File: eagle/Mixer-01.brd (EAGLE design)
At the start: 95 x 72 mm, 58 parts, among them IC1 TL072P, IC2 TL072P, IC3 LM4558N

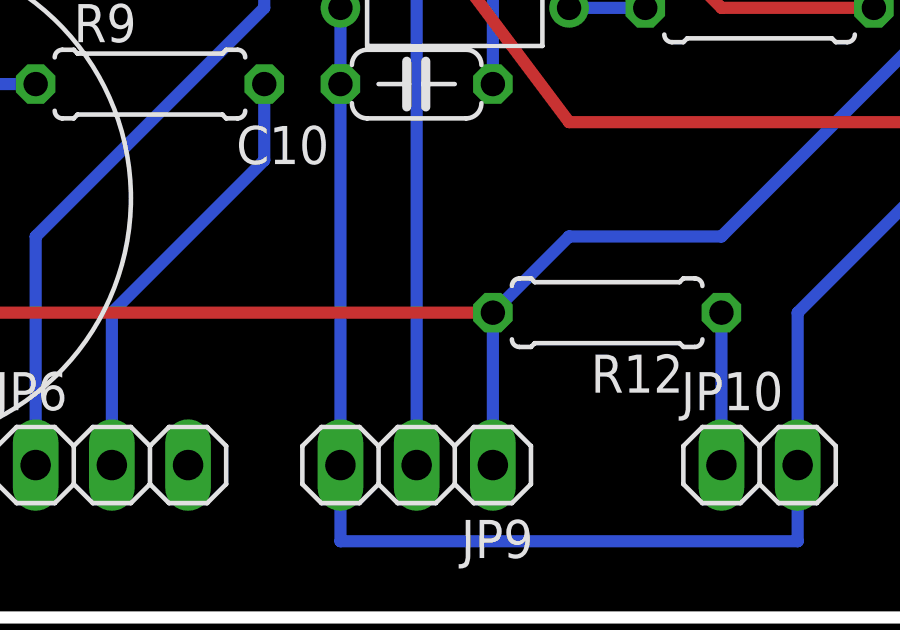
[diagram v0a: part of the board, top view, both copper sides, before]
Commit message: 電池ボックスのGNDの配線を変更
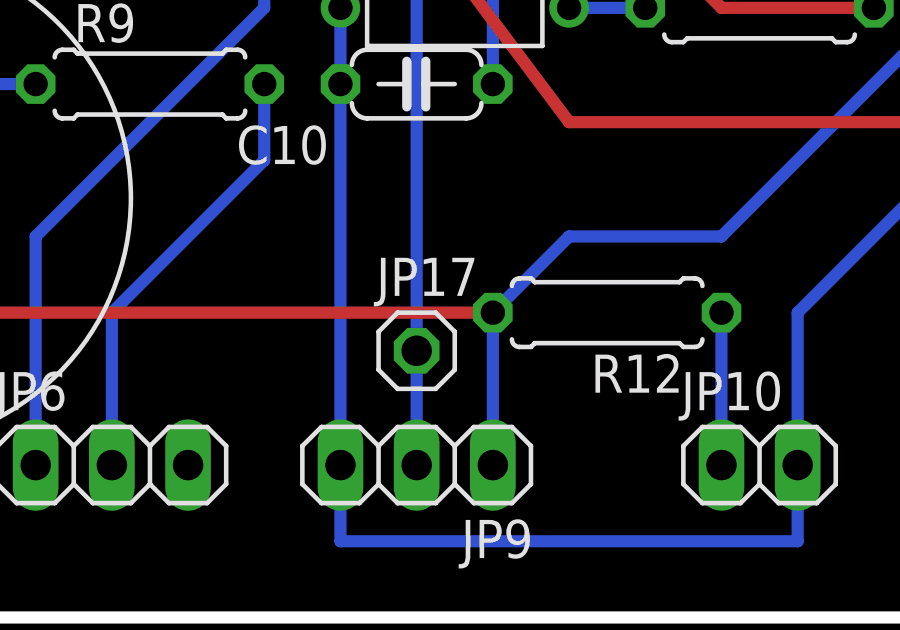
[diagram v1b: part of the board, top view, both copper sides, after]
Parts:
- added JP17: PWR-GND, pinhead:1X01
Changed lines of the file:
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@@
 <element name="R23" library="resistor" package="0207/7" value="47" x="80.01" y="33.02"/>
 <element name="JP16" library="pinhead" package="1X03" value="VOL-R" x="66.04" y="5.08"/>
+<element name="JP17" library="pinhead" package="1X01" value="PWR-GND" x="45.72" y="8.89"/>
 </elements>
 <signals>

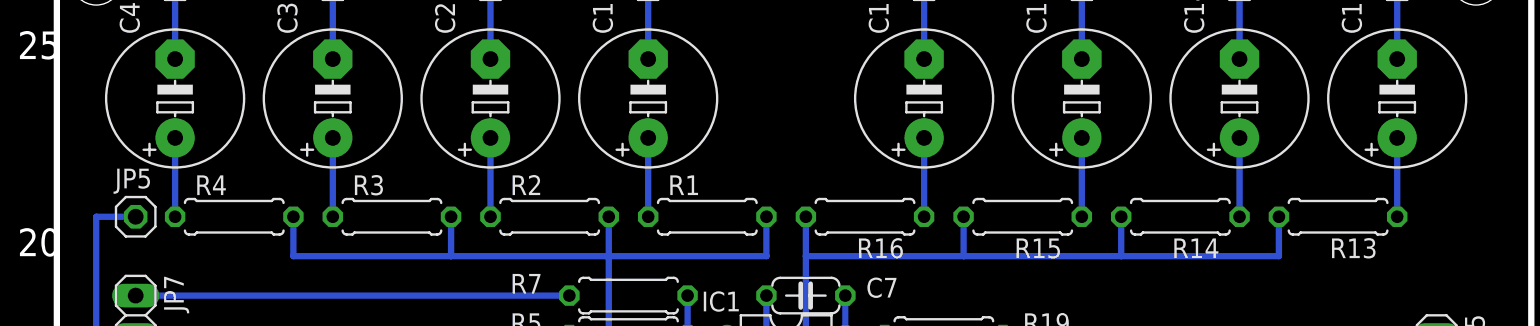
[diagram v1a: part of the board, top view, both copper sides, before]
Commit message: OPAMPの入力を接地
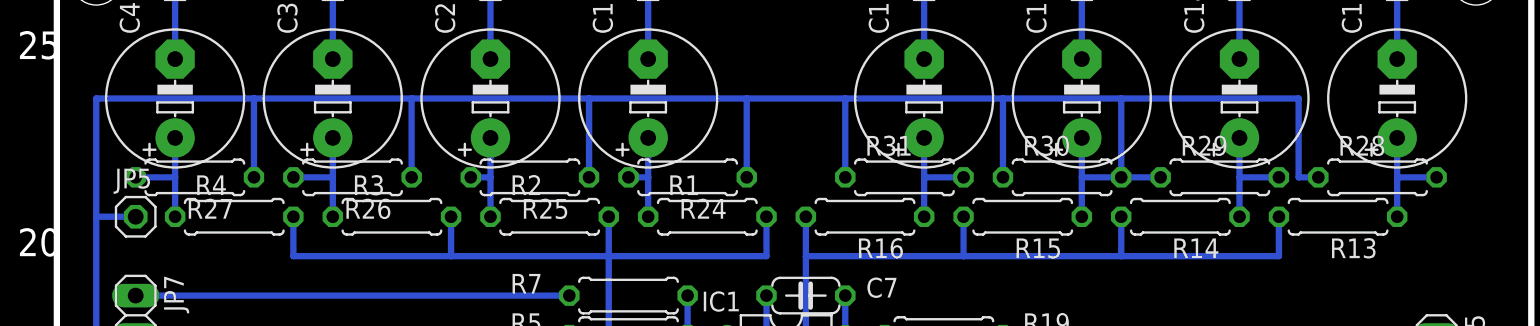
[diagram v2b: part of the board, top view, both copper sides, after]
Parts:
- added R24, R25, R26, R27, R28, R29, R30, R31: 100k, rcl:0207/7
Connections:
- net GND: now also R24.1, R25.1, R26.1, R27.1, R28.1, R29.1, R30.1, R31.1
- net N$10: now also R25.2
- net N$11: now also R26.2
- net N$12: now also R27.2
- net N$18: now also R30.2
- net N$23: now also R31.2
- net N$7: now also R28.2
- net N$8: now also R29.2
- net N$9: now also R24.2
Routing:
- net GND: track 263.0 -> 392.6 mm
- net N$7: track 5.08 -> 7.62 mm
- net N$11: track 5.08 -> 7.62 mm
- net N$12: track 5.08 -> 7.62 mm
- net N$23: track 5.08 -> 7.62 mm
- net N$8: track 5.08 -> 7.62 mm
- net N$18: track 5.08 -> 7.62 mm
- net N$9: track 5.08 -> 6.35 mm
- net N$10: track 5.08 -> 6.35 mm
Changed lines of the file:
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@@
 <layer number="97" name="Info" color="7" fill="1" visible="no" active="no"/>
 <layer number="98" name="Guide" color="6" fill="1" visible="no" active="no"/>
-<layer number="100" name="Grid" color="7" fill="1" visible="yes" active="yes"/>
+<layer number="100" name="Grid" color="7" fill="1" visible="no" active="yes"/>
 <layer number="101" name="Jumper" color="14" fill="1" visible="yes" active="yes"/>
 <layer number="102" name="outline" color="15" fill="1" visible="yes" active="yes"/>
@@
 <element name="JP16" library="pinhead" package="1X03" value="VOL-R" x="66.04" y="5.08"/>
 <element name="JP17" library="pinhead" package="1X01" value="PWR-GND" x="45.72" y="8.89"/>
+<element name="R24" library="rcl" package="0207/7" value="100k" x="40.64" y="55.88" rot="R180"/>
+<element name="R25" library="rcl" package="0207/7" value="100k" x="30.48" y="55.88" rot="R180"/>
+<element name="R26" library="rcl" package="0207/7" value="100k" x="19.05" y="55.88" rot="R180"/>
+<element name="R27" library="rcl" package="0207/7" value="100k" x="8.89" y="55.88" rot="R180"/>
+<element name="R28" library="rcl" package="0207/7" value="100k" x="85.09" y="55.88"/>
+<element name="R29" library="rcl" package="0207/7" value="100k" x="74.93" y="55.88"/>
+<element name="R30" library="rcl" package="0207/7" value="100k" x="64.77" y="55.88"/>
+<element name="R31" library="rcl" package="0207/7" value="100k" x="54.61" y="55.88"/>
 </elements>
 <signals>
@@
 <wire x1="91.44" y1="43.18" x2="88.9" y2="43.18" width="0.4064" layer="16"/>
 <wire x1="48.26" y1="35.56" x2="45.72" y2="35.56" width="0.4064" layer="16"/>
-<wire x1="5.08" y1="53.34" x2="2.54" y2="53.34" width="0.4064" layer="16"/>
 <wire x1="2.54" y1="53.34" x2="2.54" y2="45.72" width="0.4064" layer="16"/>
 <wire x1="2.54" y1="45.72" x2="5.08" y2="45.72" width="0.4064" layer="16"/>
@@
 <wire x1="27.94" y1="27.94" x2="22.86" y2="27.94" width="0.4064" layer="16"/>
 <wire x1="22.86" y1="27.94" x2="5.08" y2="45.72" width="0.4064" layer="16"/>
+<contactref element="R24" pad="1"/>
+<contactref element="R25" pad="1"/>
+<contactref element="R26" pad="1"/>
+<contactref element="R27" pad="1"/>
+<contactref element="R28" pad="1"/>
+<contactref element="R29" pad="1"/>
+<contactref element="R30" pad="1"/>
+<contactref element="R31" pad="1"/>
+<wire x1="5.08" y1="53.34" x2="2.54" y2="53.34" width="0.4064" layer="16"/>
+<wire x1="2.54" y1="53.34" x2="2.54" y2="60.96" width="0.4064" layer="16"/>
+<wire x1="2.54" y1="60.96" x2="12.7" y2="60.96" width="0.4064" layer="16"/>
+<wire x1="12.7" y1="60.96" x2="12.7" y2="55.88" width="0.4064" layer="16"/>
+<wire x1="22.86" y1="55.88" x2="22.86" y2="60.96" width="0.4064" layer="16"/>
+<wire x1="22.86" y1="60.96" x2="12.7" y2="60.96" width="0.4064" layer="16"/>
+<wire x1="34.29" y1="55.88" x2="34.29" y2="60.96" width="0.4064" layer="16"/>
+<wire x1="34.29" y1="60.96" x2="22.86" y2="60.96" width="0.4064" layer="16"/>
+<wire x1="44.45" y1="55.88" x2="44.45" y2="60.96" width="0.4064" layer="16"/>
+<wire x1="44.45" y1="60.96" x2="34.29" y2="60.96" width="0.4064" layer="16"/>
+<wire x1="50.8" y1="55.88" x2="50.8" y2="60.96" width="0.4064" layer="16"/>
+<wire x1="50.8" y1="60.96" x2="44.45" y2="60.96" width="0.4064" layer="16"/>
+<wire x1="60.96" y1="55.88" x2="60.96" y2="60.96" width="0.4064" layer="16"/>
+<wire x1="60.96" y1="60.96" x2="50.8" y2="60.96" width="0.4064" layer="16"/>
+<wire x1="71.12" y1="55.88" x2="68.58" y2="55.88" width="0.4064" layer="16"/>
+<wire x1="68.58" y1="55.88" x2="68.58" y2="60.96" width="0.4064" layer="16"/>
+<wire x1="68.58" y1="60.96" x2="60.96" y2="60.96" width="0.4064" layer="16"/>
+<wire x1="81.28" y1="55.88" x2="80.01" y2="55.88" width="0.4064" layer="16"/>
+<wire x1="80.01" y1="55.88" x2="80.01" y2="60.96" width="0.4064" layer="16"/>
+<wire x1="80.01" y1="60.96" x2="68.58" y2="60.96" width="0.4064" layer="16"/>
 </signal>
 <signal name="N$9">
 <contactref element="C1" pad="+"/>
 <contactref element="R1" pad="1"/>
-<wire x1="38.1" y1="58.42" x2="38.1" y2="53.34" width="0.4064" layer="16"/>
+<wire x1="38.1" y1="58.42" x2="38.1" y2="55.88" width="0.4064" layer="16"/>
+<contactref element="R24" pad="2"/>
+<wire x1="38.1" y1="55.88" x2="38.1" y2="53.34" width="0.4064" layer="16"/>
+<wire x1="36.83" y1="55.88" x2="38.1" y2="55.88" width="0.4064" layer="16"/>
 </signal>
 <signal name="N$10">
 <contactref element="C2" pad="+"/>
 <contactref element="R2" pad="1"/>
-<wire x1="27.94" y1="58.42" x2="27.94" y2="53.34" width="0.4064" layer="16"/>
+<wire x1="27.94" y1="58.42" x2="27.94" y2="55.88" width="0.4064" layer="16"/>
+<contactref element="R25" pad="2"/>
+<wire x1="27.94" y1="55.88" x2="27.94" y2="53.34" width="0.4064" layer="16"/>
+<wire x1="26.67" y1="55.88" x2="27.94" y2="55.88" width="0.4064" layer="16"/>
 </signal>
 <signal name="N$11">
 <contactref element="C3" pad="+"/>
 <contactref element="R3" pad="1"/>
-<wire x1="17.78" y1="58.42" x2="17.78" y2="53.34" width="0.4064" layer="16"/>
+<wire x1="17.78" y1="58.42" x2="17.78" y2="55.88" width="0.4064" layer="16"/>
+<contactref element="R26" pad="2"/>
+<wire x1="17.78" y1="55.88" x2="17.78" y2="53.34" width="0.4064" layer="16"/>
+<wire x1="15.24" y1="55.88" x2="17.78" y2="55.88" width="0.4064" layer="16"/>
 </signal>
 <signal name="N$12">
 <contactref element="C4" pad="+"/>
 <contactref element="R4" pad="1"/>
-<wire x1="7.62" y1="58.42" x2="7.62" y2="53.34" width="0.4064" layer="16"/>
+<wire x1="7.62" y1="58.42" x2="7.62" y2="55.88" width="0.4064" layer="16"/>
+<contactref element="R27" pad="2"/>
+<wire x1="7.62" y1="55.88" x2="7.62" y2="53.34" width="0.4064" layer="16"/>
+<wire x1="5.08" y1="55.88" x2="7.62" y2="55.88" width="0.4064" layer="16"/>
 </signal>
 <signal name="N$13">
@@
 <contactref element="C13" pad="+"/>
 <contactref element="R13" pad="1"/>
-<wire x1="86.36" y1="58.42" x2="86.36" y2="53.34" width="0.4064" layer="16"/>
+<wire x1="86.36" y1="58.42" x2="86.36" y2="55.88" width="0.4064" layer="16"/>
+<contactref element="R28" pad="2"/>
+<wire x1="86.36" y1="55.88" x2="86.36" y2="53.34" width="0.4064" layer="16"/>
+<wire x1="88.9" y1="55.88" x2="86.36" y2="55.88" width="0.4064" layer="16"/>
 </signal>
 <signal name="N$8">
 <contactref element="C14" pad="+"/>
 <contactref element="R14" pad="1"/>
-<wire x1="76.2" y1="58.42" x2="76.2" y2="53.34" width="0.4064" layer="16"/>
+<wire x1="76.2" y1="58.42" x2="76.2" y2="55.88" width="0.4064" layer="16"/>
+<contactref element="R29" pad="2"/>
+<wire x1="76.2" y1="55.88" x2="76.2" y2="53.34" width="0.4064" layer="16"/>
+<wire x1="78.74" y1="55.88" x2="76.2" y2="55.88" width="0.4064" layer="16"/>
 </signal>
 <signal name="N$18">
 <contactref element="C15" pad="+"/>
 <contactref element="R15" pad="1"/>
-<wire x1="66.04" y1="58.42" x2="66.04" y2="53.34" width="0.4064" layer="16"/>
+<wire x1="66.04" y1="58.42" x2="66.04" y2="55.88" width="0.4064" layer="16"/>
+<contactref element="R30" pad="2"/>
+<wire x1="66.04" y1="55.88" x2="66.04" y2="53.34" width="0.4064" layer="16"/>
+<wire x1="68.58" y1="55.88" x2="66.04" y2="55.88" width="0.4064" layer="16"/>
 </signal>
 <signal name="N$23">
 <contactref element="C16" pad="+"/>
 <contactref element="R16" pad="1"/>
-<wire x1="55.88" y1="58.42" x2="55.88" y2="53.34" width="0.4064" layer="16"/>
+<wire x1="55.88" y1="58.42" x2="55.88" y2="55.88" width="0.4064" layer="16"/>
+<contactref element="R31" pad="2"/>
+<wire x1="55.88" y1="55.88" x2="55.88" y2="53.34" width="0.4064" layer="16"/>
+<wire x1="58.42" y1="55.88" x2="55.88" y2="55.88" width="0.4064" layer="16"/>
 </signal>
 <signal name="N$24">

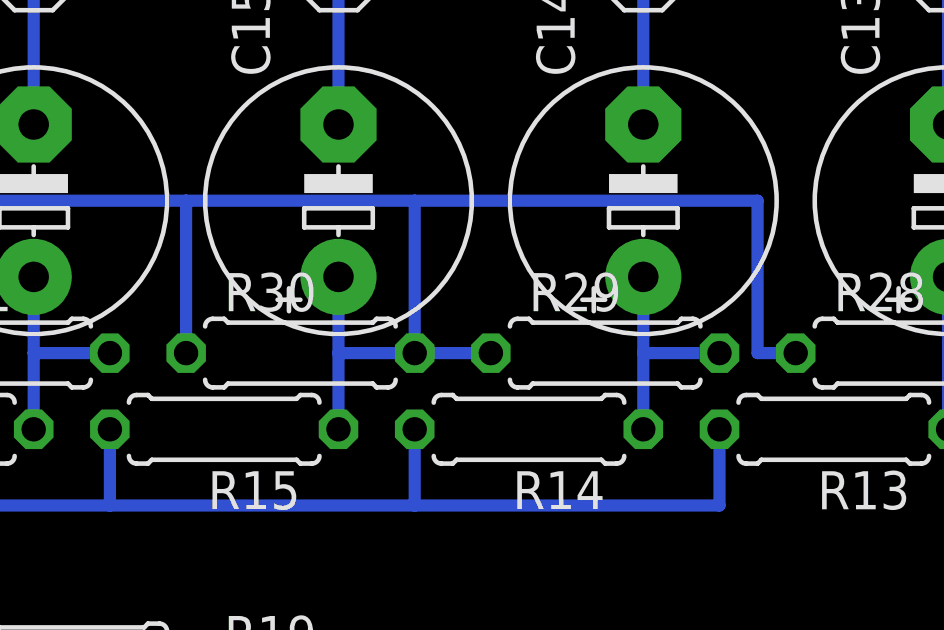
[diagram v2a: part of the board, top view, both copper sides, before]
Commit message: Mixer-01.brd: 配線を修正
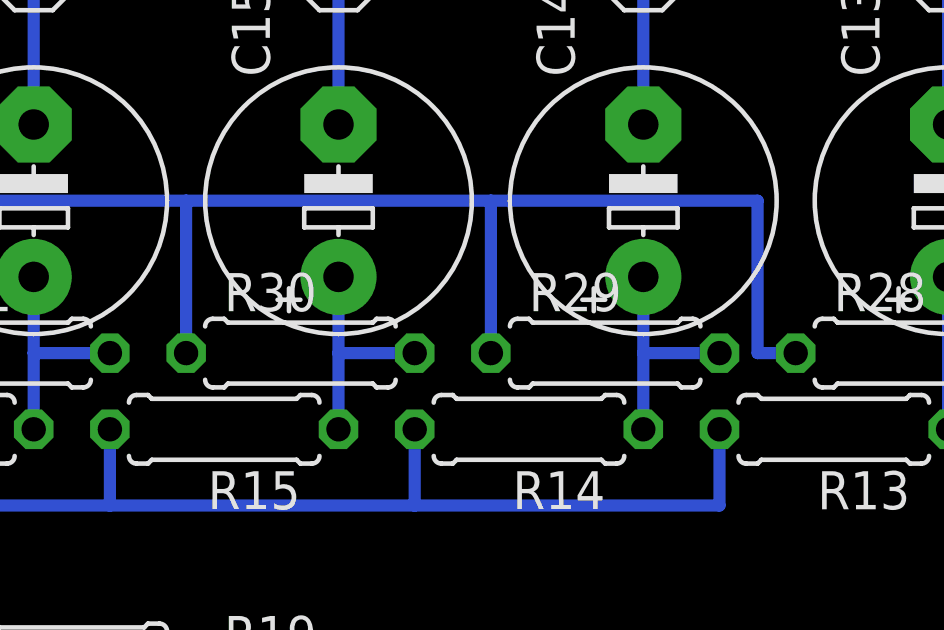
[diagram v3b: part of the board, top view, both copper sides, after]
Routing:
- net GND: track 392.6 -> 390.0 mm
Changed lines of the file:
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@@
 <wire x1="60.96" y1="55.88" x2="60.96" y2="60.96" width="0.4064" layer="16"/>
 <wire x1="60.96" y1="60.96" x2="50.8" y2="60.96" width="0.4064" layer="16"/>
-<wire x1="71.12" y1="55.88" x2="68.58" y2="55.88" width="0.4064" layer="16"/>
-<wire x1="68.58" y1="55.88" x2="68.58" y2="60.96" width="0.4064" layer="16"/>
-<wire x1="68.58" y1="60.96" x2="60.96" y2="60.96" width="0.4064" layer="16"/>
 <wire x1="81.28" y1="55.88" x2="80.01" y2="55.88" width="0.4064" layer="16"/>
 <wire x1="80.01" y1="55.88" x2="80.01" y2="60.96" width="0.4064" layer="16"/>
-<wire x1="80.01" y1="60.96" x2="68.58" y2="60.96" width="0.4064" layer="16"/>
+<wire x1="80.01" y1="60.96" x2="71.12" y2="60.96" width="0.4064" layer="16"/>
+<wire x1="71.12" y1="60.96" x2="60.96" y2="60.96" width="0.4064" layer="16"/>
+<wire x1="71.12" y1="55.88" x2="71.12" y2="60.96" width="0.4064" layer="16"/>
 </signal>
 <signal name="N$9">
@@
 <contactref element="C14" pad="+"/>
 <contactref element="R14" pad="1"/>
-<wire x1="76.2" y1="58.42" x2="76.2" y2="55.88" width="0.4064" layer="16"/>
 <contactref element="R29" pad="2"/>
-<wire x1="76.2" y1="55.88" x2="76.2" y2="53.34" width="0.4064" layer="16"/>
+<wire x1="76.2" y1="53.34" x2="76.2" y2="55.88" width="0.4064" layer="16"/>
+<wire x1="76.2" y1="55.88" x2="76.2" y2="58.42" width="0.4064" layer="16"/>
 <wire x1="78.74" y1="55.88" x2="76.2" y2="55.88" width="0.4064" layer="16"/>
 </signal>
@@
 <contactref element="C15" pad="+"/>
 <contactref element="R15" pad="1"/>
+<contactref element="R30" pad="2"/>
 <wire x1="66.04" y1="58.42" x2="66.04" y2="55.88" width="0.4064" layer="16"/>
-<contactref element="R30" pad="2"/>
 <wire x1="66.04" y1="55.88" x2="66.04" y2="53.34" width="0.4064" layer="16"/>
 <wire x1="68.58" y1="55.88" x2="66.04" y2="55.88" width="0.4064" layer="16"/>

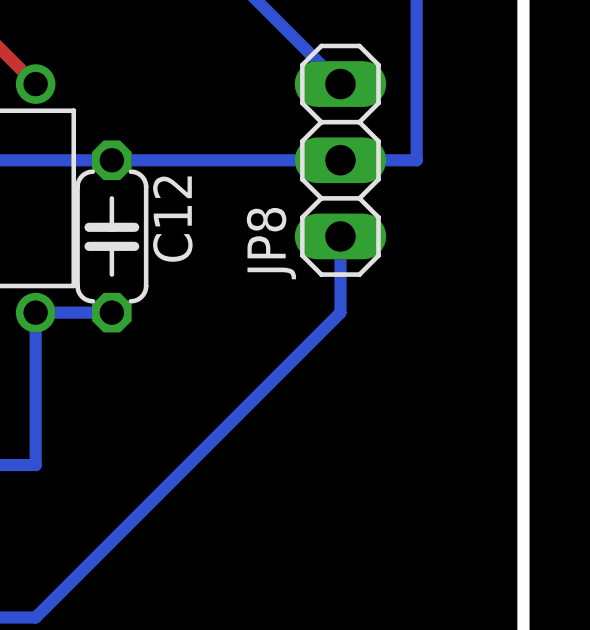
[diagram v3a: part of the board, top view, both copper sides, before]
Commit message: Mixer基板設計図にV-GND用ピンを追加
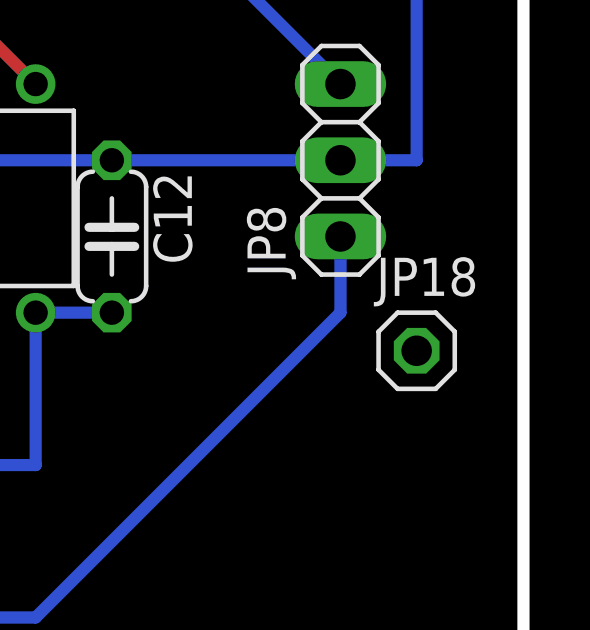
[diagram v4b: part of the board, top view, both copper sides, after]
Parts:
- added JP18: V-GND, pinhead:1X01
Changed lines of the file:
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@@
 <element name="R30" library="rcl" package="0207/7" value="100k" x="64.77" y="55.88"/>
 <element name="R31" library="rcl" package="0207/7" value="100k" x="54.61" y="55.88"/>
+<element name="JP18" library="pinhead" package="1X01" value="V-GND" x="91.44" y="19.05"/>
 </elements>
 <signals>
@@
 <contactref element="R11" pad="2"/>
 <wire x1="71.12" y1="10.16" x2="78.74" y2="10.16" width="0.4064" layer="16"/>
+<wire x1="88.9" y1="20.32" x2="78.74" y2="10.16" width="0.4064" layer="16"/>
 <wire x1="88.9" y1="22.86" x2="88.9" y2="20.32" width="0.4064" layer="16"/>
-<wire x1="88.9" y1="20.32" x2="78.74" y2="10.16" width="0.4064" layer="16"/>
 </signal>
 <signal name="N$1">
